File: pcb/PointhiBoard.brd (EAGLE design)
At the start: 110 x 60 mm, 104 parts, among them IC1 MCP7940NMSOP8, IC2 ADP2303ARDZ-5.0, IC3 IRF7240, IC4 IRF7240, IC6 4052D, IC7 ADR02, J1 22-27-2021-02, Q1 BSS123, Q2 BSS123, Q3 BSS123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

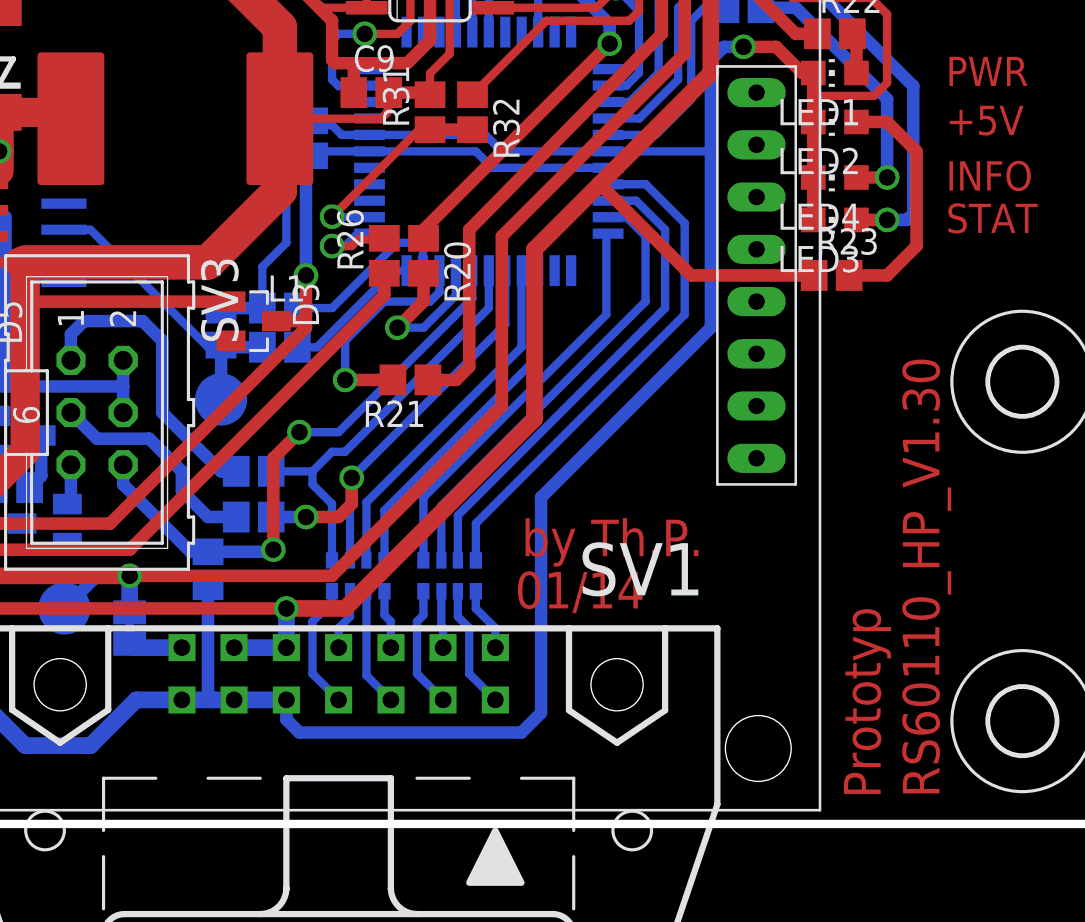
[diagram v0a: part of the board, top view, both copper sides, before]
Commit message: fix wrong adc-port, little layout modifies
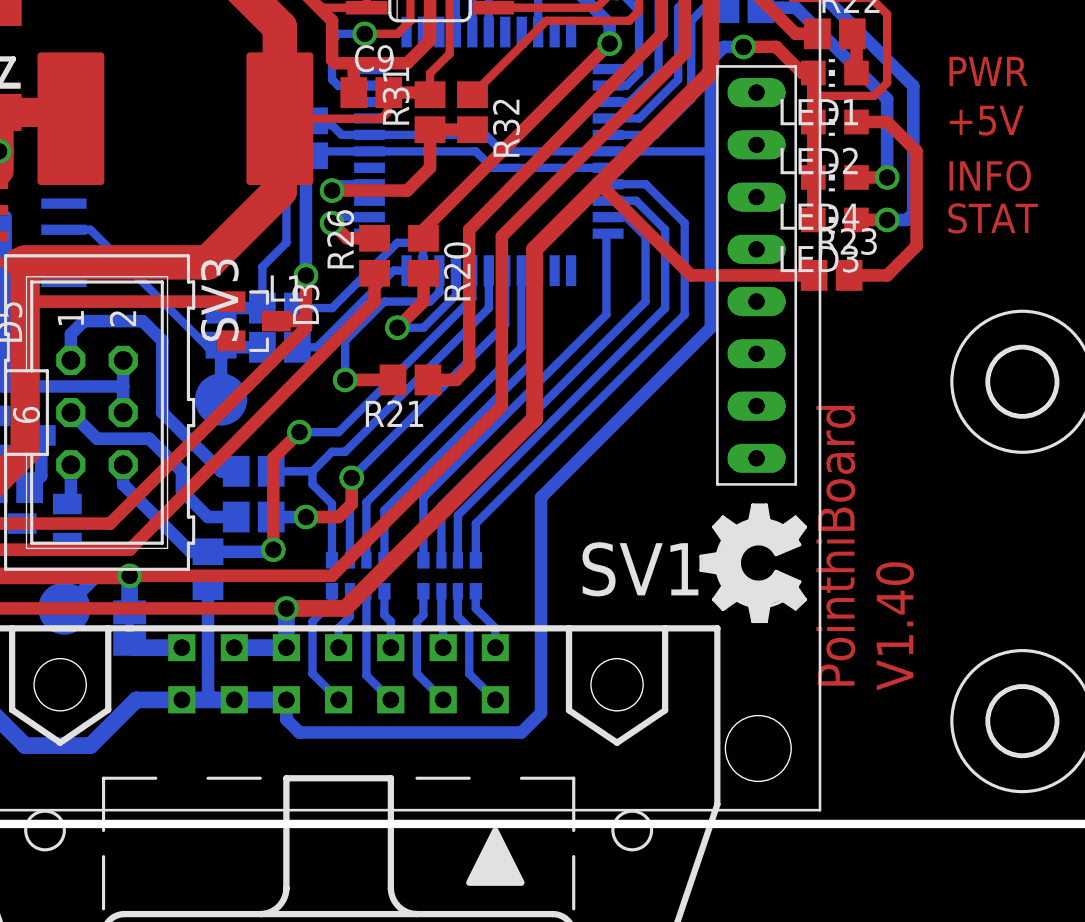
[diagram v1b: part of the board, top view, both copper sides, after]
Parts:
- added U$7: (no value), ohw-logo:OSHW_FILLX200_NOTEXT
- moved R26 0.48 mm to (73.5, 27.6)
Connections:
- removed net RA4: IC5.23, R26.2
- new net AN4: IC5.24, R26.2
- net N$60: now also IC5.26; no longer IC5.24
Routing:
- net RA4: track 4.76 -> 0.00 mm, vias 1 -> 0
- net AN4: track 0.00 -> 4.31 mm, vias 0 -> 1
- net N$60: track 10.5 -> 11.1 mm
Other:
- board text added: "PointhiBoard"
- board text added: "V1.40"
- board text removed: "01/14"
- board text removed: "Prototyp"
- board text removed: "RS60110_HP_V1.30"
- board text removed: "by Th.P."
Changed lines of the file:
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@@
 <layer number="98" name="Guide" color="6" fill="1" visible="no" active="no"/>
 <layer number="100" name="Mechanical" color="7" fill="1" visible="no" active="yes"/>
+<layer number="101" name="DRAWREF" color="11" fill="1" visible="no" active="yes"/>
+<layer number="102" name="Vscore" color="7" fill="1" visible="yes" active="yes"/>
+<layer number="103" name="tMap" color="7" fill="1" visible="yes" active="yes"/>
+<layer number="104" name="Name" color="16" fill="1" visible="yes" active="yes"/>
+<layer number="105" name="tPlate" color="7" fill="1" visible="yes" active="yes"/>
+<layer number="106" name="bPlate" color="7" fill="1" visible="yes" active="yes"/>
+<layer number="107" name="Crop" color="7" fill="1" visible="yes" active="yes"/>
+<layer number="116" name="Patch_BOT" color="9" fill="4" visible="yes" active="yes"/>
+<layer number="121" name="_tsilk" color="7" fill="1" visible="yes" active="yes"/>
+<layer number="122" name="_bsilk" color="7" fill="1" visible="yes" active="yes"/>
+<layer number="144" name="DrillLegend" color="7" fill="1" visible="no" active="yes"/>
 <layer number="151" name="HeatSink" color="7" fill="1" visible="no" active="yes"/>
 <layer number="200" name="200bmp" color="7" fill="1" visible="no" active="yes"/>
+<layer number="201" name="201bmp" color="2" fill="10" visible="no" active="yes"/>
+<layer number="202" name="202bmp" color="3" fill="10" visible="no" active="yes"/>
+<layer number="203" name="203bmp" color="4" fill="10" visible="no" active="yes"/>
+<layer number="204" name="204bmp" color="5" fill="10" visible="no" active="yes"/>
+<layer number="205" name="205bmp" color="6" fill="10" visible="no" active="yes"/>
+<layer number="206" name="206bmp" color="7" fill="10" visible="no" active="yes"/>
+<layer number="207" name="207bmp" color="15" fill="10" visible="no" active="yes"/>
+<layer number="208" name="208bmp" color="9" fill="10" visible="yes" active="yes"/>
+<layer number="209" name="209bmp" color="7" fill="1" visible="yes" active="yes"/>
+<layer number="210" name="210bmp" color="7" fill="1" visible="yes" active="yes"/>
+<layer number="211" name="211bmp" color="7" fill="1" visible="yes" active="yes"/>
+<layer number="212" name="212bmp" color="7" fill="1" visible="yes" active="yes"/>
+<layer number="213" name="213bmp" color="7" fill="1" visible="yes" active="yes"/>
+<layer number="214" name="214bmp" color="7" fill="1" visible="yes" active="yes"/>
+<layer number="215" name="215bmp" color="7" fill="1" visible="yes" active="yes"/>
+<layer number="216" name="216bmp" color="7" fill="1" visible="yes" active="yes"/>
 <layer number="231" name="Eagle3D_PG1" color="7" fill="1" visible="no" active="yes"/>
 <layer number="232" name="Eagle3D_PG2" color="7" fill="1" visible="no" active="yes"/>
@@
 <wire x1="110" y1="60" x2="0" y2="60" width="0.4064" layer="20"/>
 <wire x1="0" y1="60" x2="0" y2="0" width="0.3048" layer="20"/>
-<text x="100.965" y="1.27" size="1.778" layer="1" font="vector" ratio="18" rot="R90">RS60110_HP_V1.30</text>
-<text x="80.645" y="13.0175" size="1.778" layer="1" font="vector" ratio="18">by Th.P.</text>
-<text x="80.3275" y="10.4775" size="1.778" layer="1" font="vector" ratio="18">01/14</text>
-<text x="98.1075" y="1.2427625" size="1.778" layer="1" font="vector" ratio="18" rot="R90">Prototyp</text>
+<text x="96.8375" y="6.50875" size="1.778" layer="1" font="vector" ratio="18" rot="R90">PointhiBoard</text>
+<text x="99.695" y="6.4815125" size="1.778" layer="1" font="vector" ratio="18" rot="R90">V1.40</text>
 <text x="101.2825" y="35.8775" size="1.4224" layer="1" font="vector" ratio="24">PWR</text>
 <text x="101.2825" y="33.49625" size="1.4224" layer="1" font="vector" ratio="24">+5V</text>
@@
 <element name="D5" library="diode" package="DO214AA" value="SSB43L" x="53.6575" y="22.86" rot="R270"/>
 <element name="C14" library="resistor" package="PANASONIC_D" value="47µ" x="40.64" y="26.67" rot="MR180"/>
-<element name="R26" library="resistor" package="R0805" value="560R" x="73.9775" y="27.6225" rot="R90"/>
+<element name="R26" library="resistor" package="R0805" value="560R" x="73.50125" y="27.6225" rot="R90"/>
 <element name="R27" library="resistor" package="R0805" value="12k" x="55.88" y="16.35125" rot="MR0"/>
 <element name="R28" library="resistor" package="R0805" value="1k5" x="53.34" y="11.1125" rot="MR315"/>
@@
 <element name="R31" library="resistor" package="R0805" value="560R" x="76.2" y="34.6075" rot="R90"/>
 <element name="R32" library="resistor" package="R0805" value="560R" x="78.26375" y="34.6075" rot="R270"/>
+<element name="U$7" library="ohw-logo" package="OSHW_FILLX200_NOTEXT" value="" x="94.45625" y="9.8425" rot="R90"/>
 </elements>
 <signals>
@@
 <wire x1="86.575" y1="55.5625" x2="86.995" y2="55.665" width="0.6096" layer="16"/>
 </signal>
-<signal name="RA4">
-<contactref element="IC5" pad="23"/>
-<contactref element="R26" pad="2"/>
-<via x="71.4375" y="28.09875" extent="1-16" drill="0.8" shape="square"/>
-<wire x1="71.4375" y1="28.09875" x2="72.39" y2="28.09875" width="0.4064" layer="1"/>
-<wire x1="72.39" y1="28.09875" x2="72.7075" y2="28.41625" width="0.4064" layer="1"/>
-<wire x1="72.7075" y1="28.41625" x2="73.92125" y2="28.41625" width="0.4064" layer="1"/>
-<wire x1="73.92125" y1="28.41625" x2="73.9775" y2="28.4725" width="0.4064" layer="1"/>
-<wire x1="73.2575" y1="28.7025" x2="72.67625" y2="28.7025" width="0.4064" layer="16"/>
-<wire x1="72.67625" y1="28.7025" x2="72.0725" y2="28.09875" width="0.4064" layer="16"/>
-<wire x1="72.0725" y1="28.09875" x2="71.4375" y2="28.09875" width="0.4064" layer="16"/>
-</signal>
 <signal name="N$58">
 <contactref element="R28" pad="1"/>
 <contactref element="R27" pad="2"/>
 <contactref element="R26" pad="1"/>
-<wire x1="73.9775" y1="26.7725" x2="73.9775" y2="25.7175" width="0.6096" layer="1"/>
-<wire x1="73.9775" y1="25.7175" x2="61.595" y2="13.335" width="0.6096" layer="1"/>
+<wire x1="73.50125" y1="26.7725" x2="73.50125" y2="25.4" width="0.6096" layer="1"/>
+<wire x1="73.50125" y1="25.4" x2="61.595" y2="13.335" width="0.6096" layer="1"/>
 <wire x1="61.595" y1="13.335" x2="52.3875" y2="13.335" width="0.6096" layer="1"/>
 <via x="52.3875" y="13.335" extent="1-16" drill="0.8" shape="square"/>
@@
 </signal>
 <signal name="N$60">
-<contactref element="IC5" pad="24"/>
 <contactref element="R31" pad="1"/>
-<wire x1="73.2575" y1="29.5025" x2="71.4625" y2="29.5025" width="0.4064" layer="16"/>
-<via x="71.4375" y="29.5275" extent="1-16" drill="0.8" shape="square"/>
 <contactref element="R32" pad="2"/>
 <wire x1="76.14375" y1="33.81375" x2="76.2" y2="33.7575" width="0.6096" layer="1"/>
 <wire x1="78.26375" y1="33.7575" x2="76.2" y2="33.7575" width="0.6096" layer="1"/>
-<wire x1="71.4625" y1="29.5025" x2="71.4375" y2="29.5275" width="0.4064" layer="16"/>
-<wire x1="71.4375" y1="29.5275" x2="75.6675" y2="33.7575" width="0.4064" layer="1"/>
-<wire x1="75.6675" y1="33.7575" x2="76.2" y2="33.7575" width="0.4064" layer="1"/>
+<wire x1="76.2" y1="33.7575" x2="76.2" y2="31.90875" width="0.6096" layer="1"/>
+<contactref element="IC5" pad="26"/>
+<wire x1="73.2575" y1="31.1025" x2="71.90125" y2="31.1025" width="0.4064" layer="16"/>
+<wire x1="71.90125" y1="31.1025" x2="71.4375" y2="30.7975" width="0.4064" layer="16"/>
+<via x="71.4375" y="30.7975" extent="1-16" drill="0.8" shape="square"/>
+<wire x1="71.4375" y1="30.7975" x2="75.08875" y2="30.7975" width="0.6096" layer="1"/>
+<wire x1="75.08875" y1="30.7975" x2="76.2" y2="31.90875" width="0.6096" layer="1"/>
 </signal>
 <signal name="+3V3">
@@
 <wire x1="22.38375" y1="35.71875" x2="19.685" y2="38.4175" width="0.6096" layer="1"/>
 </signal>
+<signal name="AN4">
+<contactref element="IC5" pad="24"/>
+<contactref element="R26" pad="2"/>
+<via x="71.4375" y="29.21" extent="1-16" drill="0.8" shape="square"/>
+<wire x1="71.4375" y1="29.21" x2="71.73" y2="29.5025" width="0.4064" layer="16"/>
+<wire x1="71.73" y1="29.5025" x2="73.2575" y2="29.5025" width="0.4064" layer="16"/>
+<wire x1="73.50125" y1="28.4725" x2="72.175" y2="28.4725" width="0.6096" layer="1"/>
+<wire x1="72.175" y1="28.4725" x2="71.4375" y2="29.21" width="0.6096" layer="1"/>
+</signal>
 </signals>
-<errors>
-</errors>
 </board>
 </drawing>

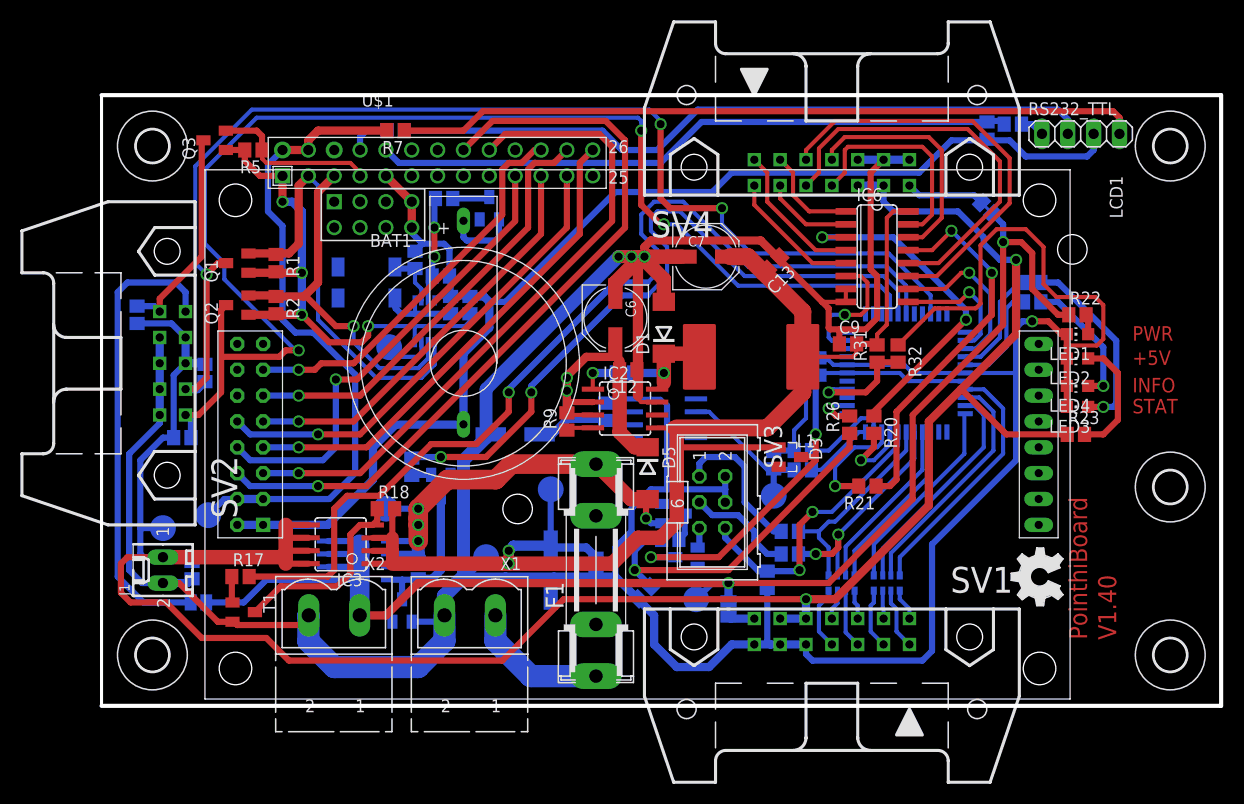
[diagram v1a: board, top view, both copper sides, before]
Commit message: fix position and orentation of text(values, names,...) on the pcb
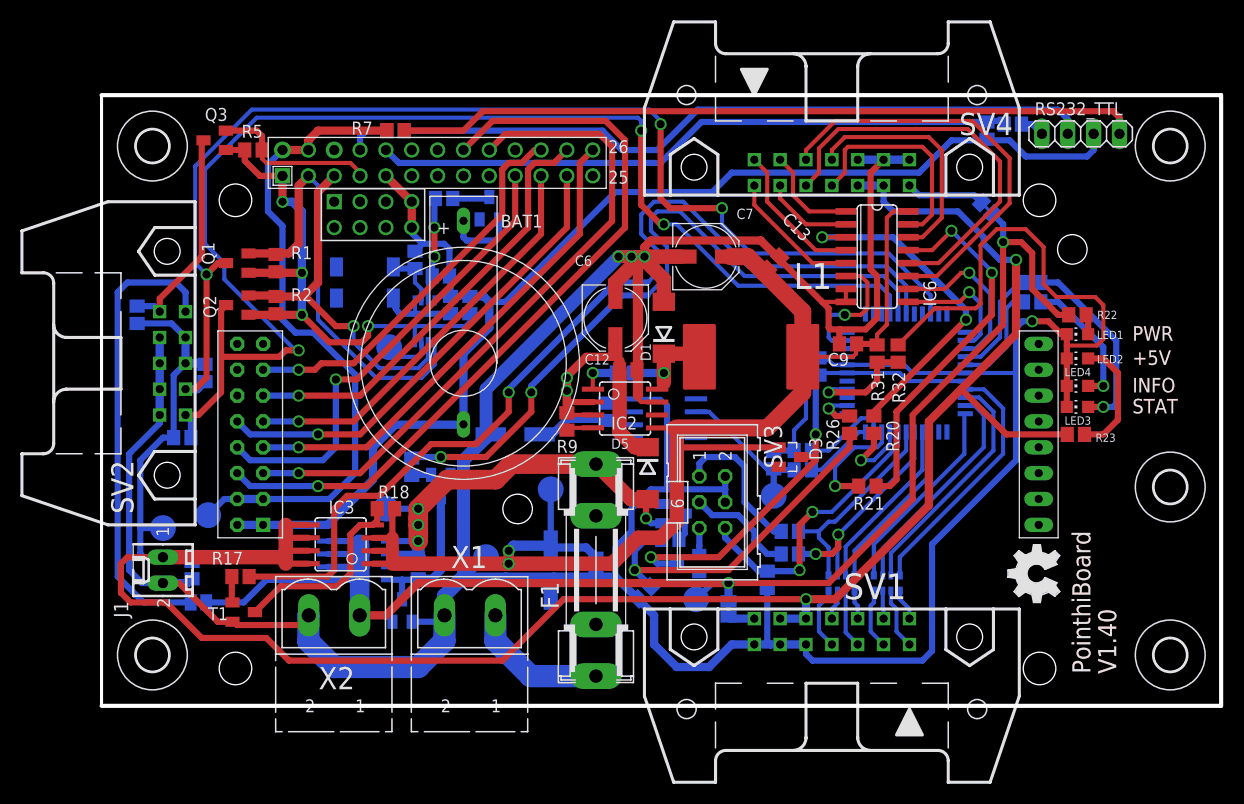
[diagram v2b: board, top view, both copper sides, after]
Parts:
- F1: value FUSESHK20L_6A -> 6A
- IC1: value MCP7940NMSOP8 -> MCP7940N
- IC5: value (none) -> 18F4420
- moved D4 0.65 mm to (57.6, 14.0)
- moved U$7 0.45 mm to (94.1, 10.2)
- moved 32.768KHZ 0.16 mm to (25.9, 41.6)
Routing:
- net N$31: track 1.98 -> 2.54 mm
